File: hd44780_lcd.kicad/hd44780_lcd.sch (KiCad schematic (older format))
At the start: 3 parts, among them U1 PIC12F675-IP, U2 74HC595

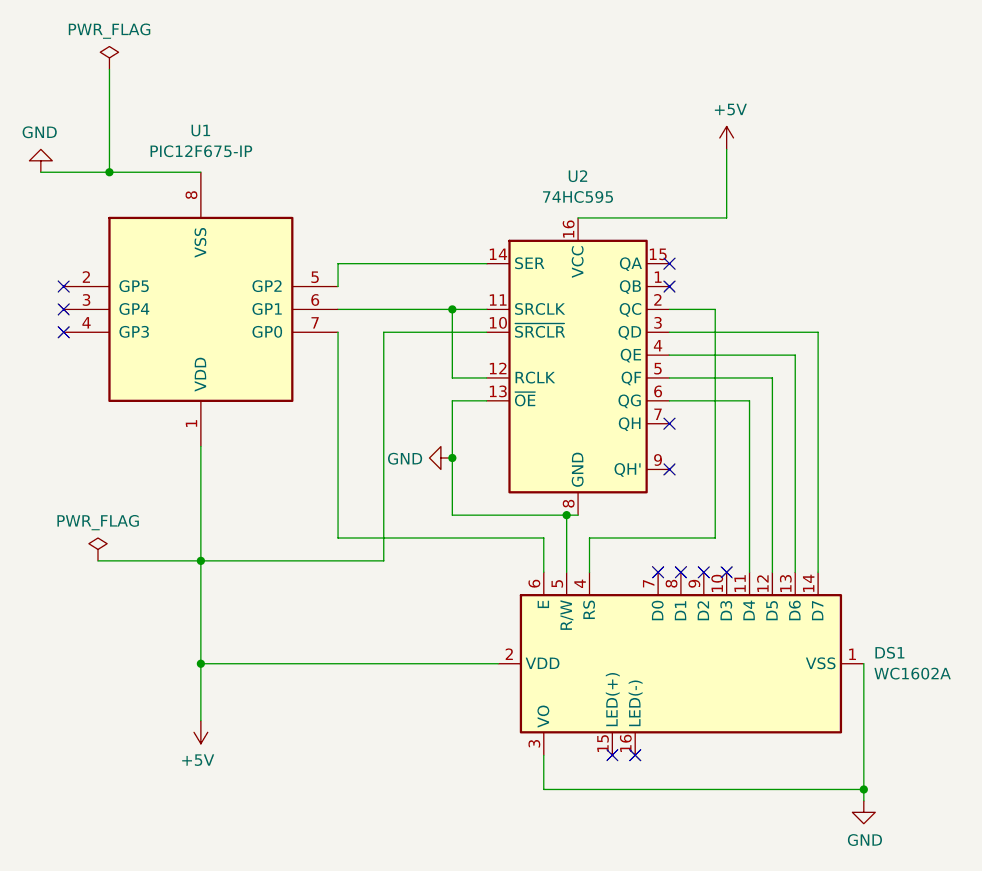
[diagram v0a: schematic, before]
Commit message: Rev 4: wire backlight pins 15 and 16
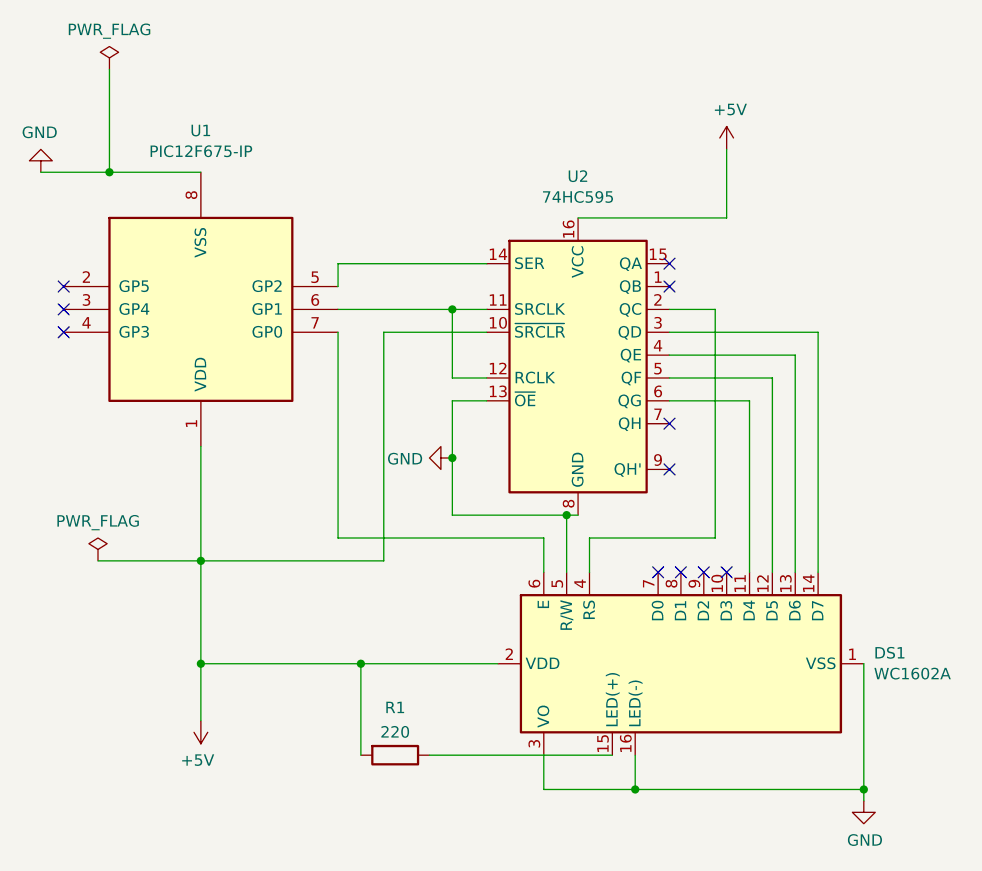
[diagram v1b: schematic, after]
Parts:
- added R1: 220, symbol Device:R
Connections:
- net +5V: now also R1.2
- net GND: now also DS1.16 (LED(-))
- net at DS1.15 (LED(+)): now also R1.1
- no-connect marks 13 -> 11
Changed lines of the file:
@@
 Title "PIC12F675 with HD44780 LCD"
 Date "2020-03-21"
-Rev "3"
+Rev "4"
 Comp "Bernhard Bablok"
 Comment1 "https://github.com/bablokb/pic-toolchain/src/hd44780_lcd"
@@
 NoConn ~ 4900 4100
 NoConn ~ 4800 4100
-NoConn ~ 4700 4900
-NoConn ~ 4600 4900
 Wire Wire Line
 	4400 4100 4400 3850
@@
 	4400 3850 3900 3850
 Wire Wire Line
-	2800 4500 4100 4500
+	2800 4500 3500 4500
 Wire Wire Line
 	5700 4500 5700 5050
 Wire Wire Line
-	4300 5050 5700 5050
+	4300 5050 4700 5050
 Wire Wire Line
 	4300 4900 4300 5050
@@
 Wire Wire Line
 	5700 5050 5700 5100
+$Comp
+L Device:R R1
+U 1 1 5E762B37
+P 3650 4900
+F 0 "R1" V 3443 4900 50  0000 C CNN
+F 1 "220" V 3550 4900 50  0000 C CNN
+F 2 "" V 3580 4900 50  0001 C CNN
+F 3 "~" H 3650 4900 50  0001 C CNN
+	1    3650 4900
+	0    1    1    0
+$EndComp
+Wire Wire Line
+	3500 4900 3500 4500
+Connection ~ 3500 4500
+Wire Wire Line
+	3500 4500 4100 4500
+Wire Wire Line
+	3800 4900 4600 4900
+Wire Wire Line
+	4700 4900 4700 5050
+Connection ~ 4700 5050
+Wire Wire Line
+	4700 5050 5700 5050
 $EndSCHEMATC

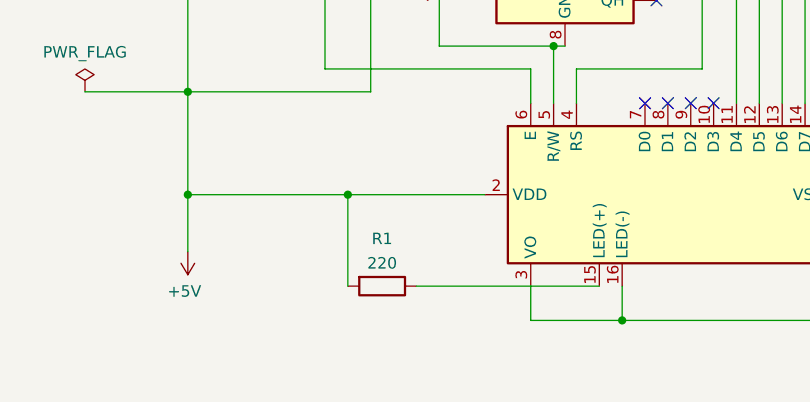
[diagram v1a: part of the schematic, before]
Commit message: Rev 5: added variable resistor for VO
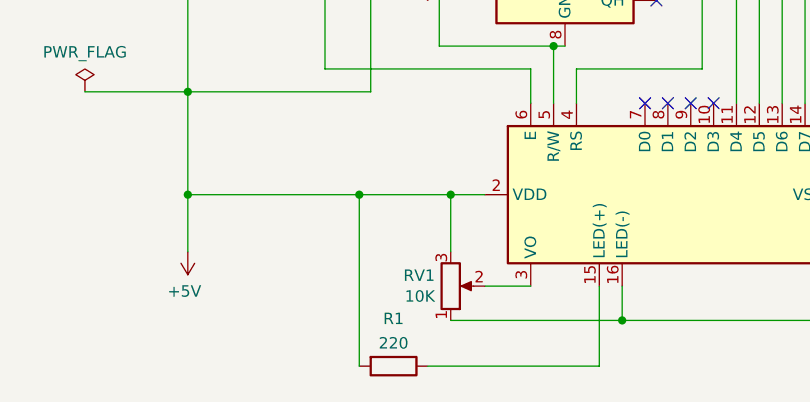
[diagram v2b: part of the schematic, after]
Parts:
- added RV1: 10K, symbol Device:R_POT
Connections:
- net +5V: now also RV1.3
- net GND: now also RV1.1; no longer DS1.3 (VO)
- new net: DS1.3 (VO), RV1.2
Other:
- moved on the sheet: R1
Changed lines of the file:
@@
 Sheet 1 1
 Title "PIC12F675 with HD44780 LCD"
-Date "2020-03-21"
-Rev "4"
+Date "2020-03-26"
+Rev "5"
 Comp "Bernhard Bablok"
 Comment1 "https://github.com/bablokb/pic-toolchain/src/hd44780_lcd"
@@
 	1    0    0    -1
 $EndComp
-$Comp
-L power:PWR_FLAG #FLG01
-U 1 1 5E7638B3
-P 2350 4050
-F 0 "#FLG01" H 2350 4125 50  0001 C CNN
-F 1 "PWR_FLAG" H 2350 4223 50  0000 C CNN
-F 2 "" H 2350 4050 50  0001 C CNN
-F 3 "~" H 2350 4050 50  0001 C CNN
-	1    2350 4050
-	1    0    0    -1
-$EndComp
 Wire Wire Line
 	2400 1900 2400 2350
@@
 Wire Wire Line
 	2400 2350 2800 2350
-Wire Wire Line
-	2350 4050 2800 4050
 NoConn ~ 4850 2750
 NoConn ~ 4850 2850
@@
 	4400 3850 3900 3850
 Wire Wire Line
-	2800 4500 3500 4500
-Wire Wire Line
 	5700 4500 5700 5050
-Wire Wire Line
-	4300 5050 4700 5050
-Wire Wire Line
-	4300 4900 4300 5050
 Connection ~ 5700 5050
 Wire Wire Line
@@
 L Device:R R1
 U 1 1 5E762B37
-P 3650 4900
-F 0 "R1" V 3443 4900 50  0000 C CNN
-F 1 "220" V 3550 4900 50  0000 C CNN
-F 2 "" V 3580 4900 50  0001 C CNN
-F 3 "~" H 3650 4900 50  0001 C CNN
-	1    3650 4900
+P 3700 5250
+F 0 "R1" V 3493 5250 50  0000 C CNN
+F 1 "220" V 3600 5250 50  0000 C CNN
+F 2 "" V 3630 5250 50  0001 C CNN
+F 3 "~" H 3700 5250 50  0001 C CNN
+	1    3700 5250
 	0    1    1    0
 $EndComp
-Wire Wire Line
-	3500 4900 3500 4500
-Connection ~ 3500 4500
-Wire Wire Line
-	3500 4500 4100 4500
-Wire Wire Line
-	3800 4900 4600 4900
 Wire Wire Line
 	4700 4900 4700 5050
@@
 Wire Wire Line
 	4700 5050 5700 5050
+Wire Wire Line
+	4600 4900 4600 5250
+Wire Wire Line
+	3550 5250 3550 4500
+Connection ~ 3550 4500
+Wire Wire Line
+	3550 4500 3950 4500
+Wire Wire Line
+	4600 5250 3850 5250
+Wire Wire Line
+	2350 4050 2800 4050
+Wire Wire Line
+	2800 4500 3550 4500
+$Comp
+L power:PWR_FLAG #FLG01
+U 1 1 5E7638B3
+P 2350 4050
+F 0 "#FLG01" H 2350 4125 50  0001 C CNN
+F 1 "PWR_FLAG" H 2350 4223 50  0000 C CNN
+F 2 "" H 2350 4050 50  0001 C CNN
+F 3 "~" H 2350 4050 50  0001 C CNN
+	1    2350 4050
+	1    0    0    -1
+$EndComp
+$Comp
+L Device:R_POT RV1
+U 1 1 5E7E7257
+P 3950 4900
+F 0 "RV1" H 3881 4854 50  0000 R CNN
+F 1 "10K" H 3881 4945 50  0000 R CNN
+F 2 "" H 3950 4900 50  0001 C CNN
+F 3 "~" H 3950 4900 50  0001 C CNN
+	1    3950 4900
+	1    0    0    1
+$EndComp
+Wire Wire Line
+	3950 5050 4700 5050
+Wire Wire Line
+	4300 4900 4100 4900
+Wire Wire Line
+	3950 4750 3950 4500
+Connection ~ 3950 4500
+Wire Wire Line
+	3950 4500 4100 4500
 $EndSCHEMATC
